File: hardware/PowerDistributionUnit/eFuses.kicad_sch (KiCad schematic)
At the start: 13 parts, among them U3 TCA9544A, U36 MCP23S17-E/SS

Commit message: schematic updated
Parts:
- removed C166: 0.1u, symbol Device:C_Small
- removed R134: R_Small, symbol Device:R_Small
- removed U36: MCP23S17-E/SS, Package_SO:SSOP-28_5.3x10.2mm_P0.65mm, symbol PowerDistributionUnitLib:MCP23S17-E/SS
- added J11, J12, J13, J18: Conn_01x02, Connector_PinHeader_2.54mm:PinHeader_1x02_P2.54mm_Vertical, symbol Connector_Generic:Conn_01x02
- C167: footprint (none) -> Capacitor_SMD:C_0603_1608Metric
- R121, R122, R123, R124, R125, R126, R127, R128: footprint (none) -> Resistor_SMD:R_0603_1608Metric
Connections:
- net SC0: now also J11.1 (Pin_1)
- net SC1: now also J12.1 (Pin_1)
- net SC2: now also J13.1 (Pin_1)
- net SC3: now also J18.1 (Pin_1)
- net SD0: now also J11.2 (Pin_2)
- net SD1: now also J12.2 (Pin_2)
- net SD2: now also J13.2 (Pin_2)
- net SD3: now also J18.2 (Pin_2)
- net R_{ILIM}_SCL renamed SDA
- net R_{ILIM}_SDA renamed SCL
- no-connect marks 9 -> 17
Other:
- removed sheet eFuseCAN
- added sheet eFuse Monitoring and Control (eFuse Monitoring and Control.kicad_sch)
- added sheet eFuse14 (eFuse.kicad_sch)
- added sheet eFuse15 (eFuse.kicad_sch)
- sheet eFuse0 ports: added IMON-; removed none
- sheet eFuse1 ports: added IMON-; removed none
- sheet eFuse10 ports: added IMON-; removed none
- sheet eFuse11 ports: added IMON-; removed none
- sheet eFuse12 ports: added IMON-; removed none
- sheet eFuse13 ports: added IMON-; removed none
- sheet eFuse2 ports: added IMON-; removed none
- sheet eFuse3 ports: added IMON-; removed none
- sheet eFuse4 ports: added IMON-; removed none
- sheet eFuse5 ports: added IMON-; removed none
- sheet eFuse6 ports: added IMON-; removed none
- sheet eFuse7 ports: added IMON-; removed none
- sheet eFuse8 ports: added IMON-; removed none
- sheet eFuse9 ports: added IMON-; removed none
- note added: "Control and Monitoring"
- note added: "Test Points"
- note removed: "0"
- note removed: "0011000"
- note removed: "0011010"
- note removed: "1"
- note removed: "1001100"
- note removed: "1001110"
- note removed: "AD0"
- note removed: "AD1"
- note removed: "ADDRESS"
- note removed: "Digital Pot not used in CAN output to maintain iso"
- note removed: "External Connections"
- note removed: "Output Enable"
- note removed: "R_{ILIM} I^{2}C Addresses"
- note removed: "to Connectors..."
- note removed: "to Control..."
- note removed: "to Monitoring..."
- company: (none) -> Longhorn Racing
- title: (none) -> eFuses
- moved on the sheet: R121, R122, R123, R124, R125, R126, R127, R128

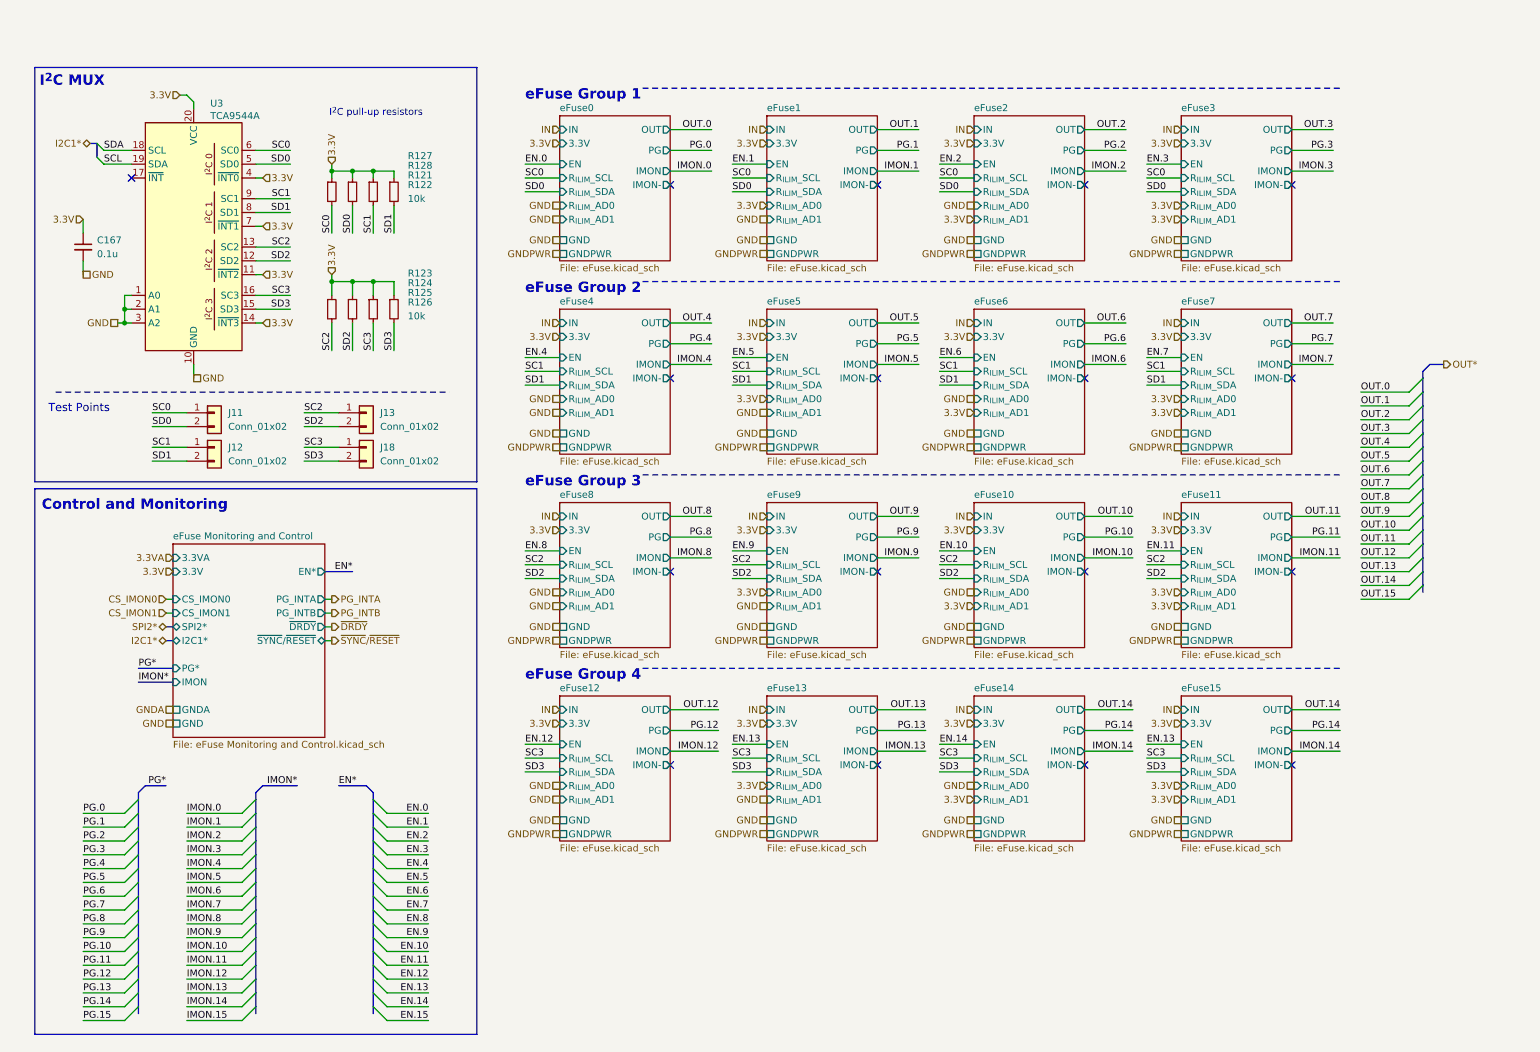
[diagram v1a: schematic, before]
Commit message: started layout for general and eFuses, corrected schematic (test point footprints, bus label names, connection points, etc.), corrected footprint courtyard (eFuse, diode)
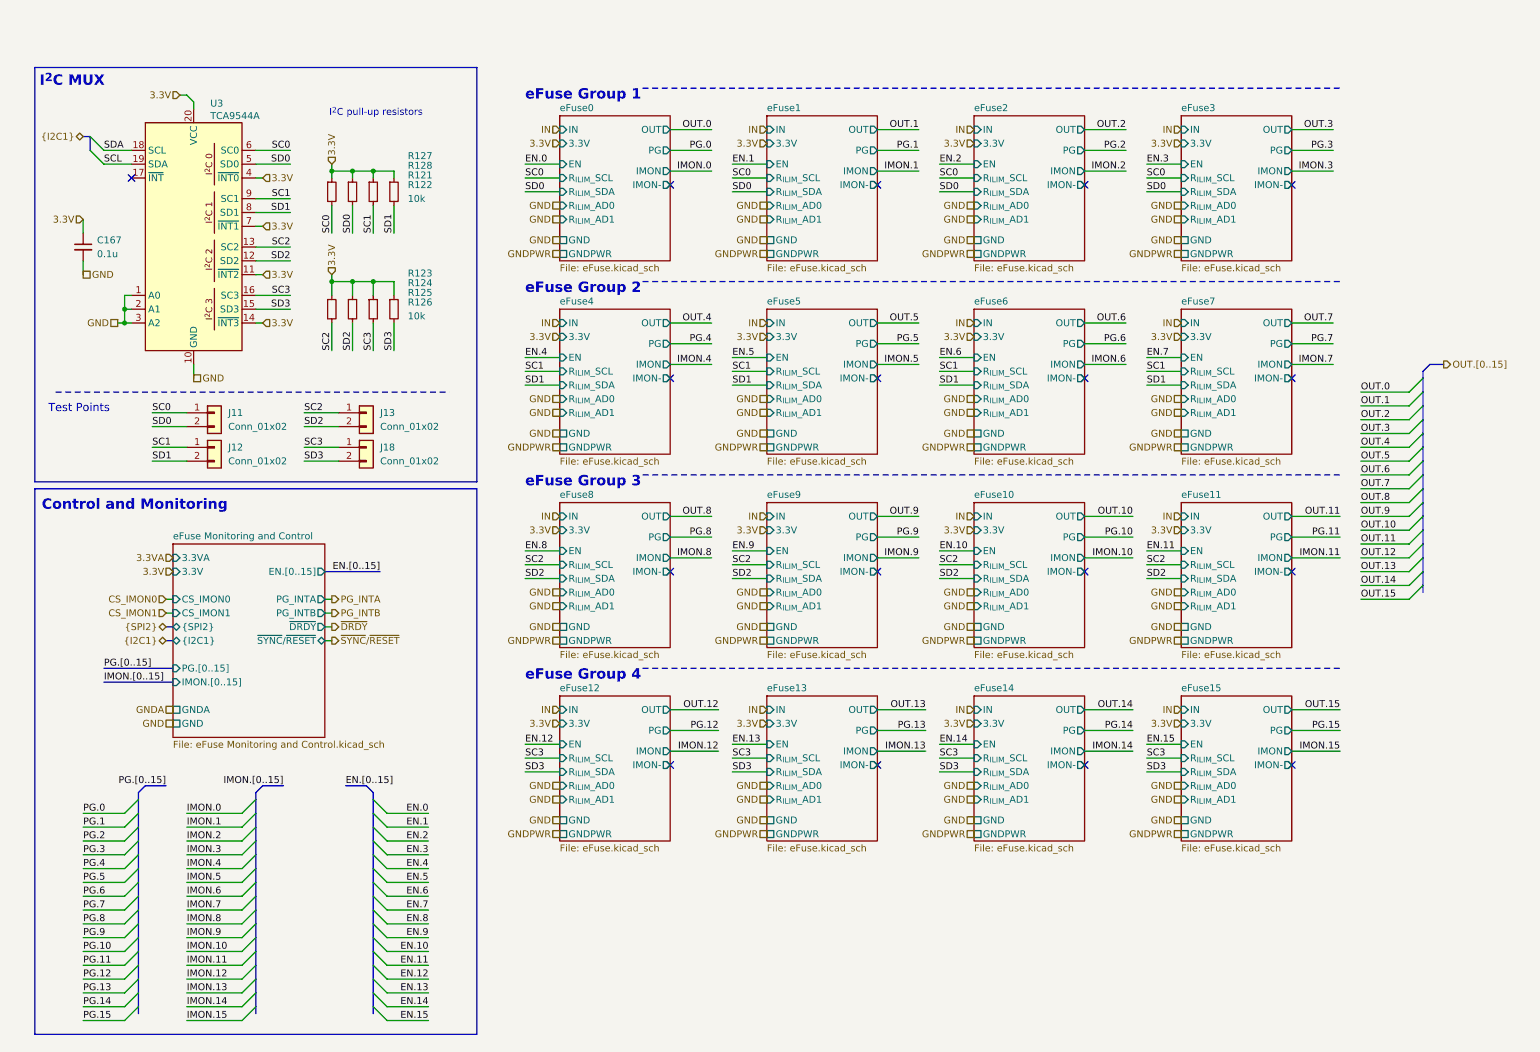
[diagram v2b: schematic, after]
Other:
- sheet eFuse Monitoring and Control ports: added EN.[0..15], IMON.[0..15], PG.[0..15], {I2C1}, {SPI2}; removed EN*, I2C1*, IMON, PG*, SPI2*

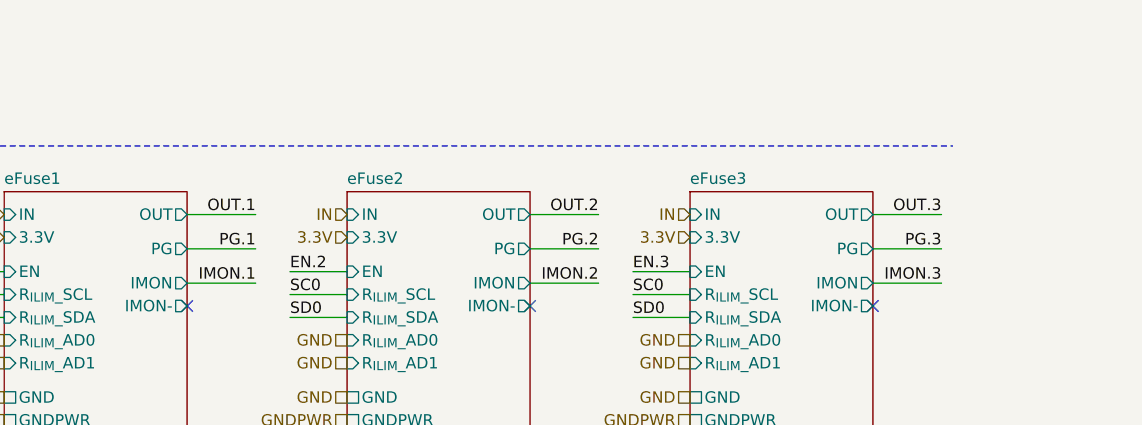
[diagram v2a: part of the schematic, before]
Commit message: Updated GND and 3.3V to GNDA and 3.3VA. Made progress on layout for current monitoring components
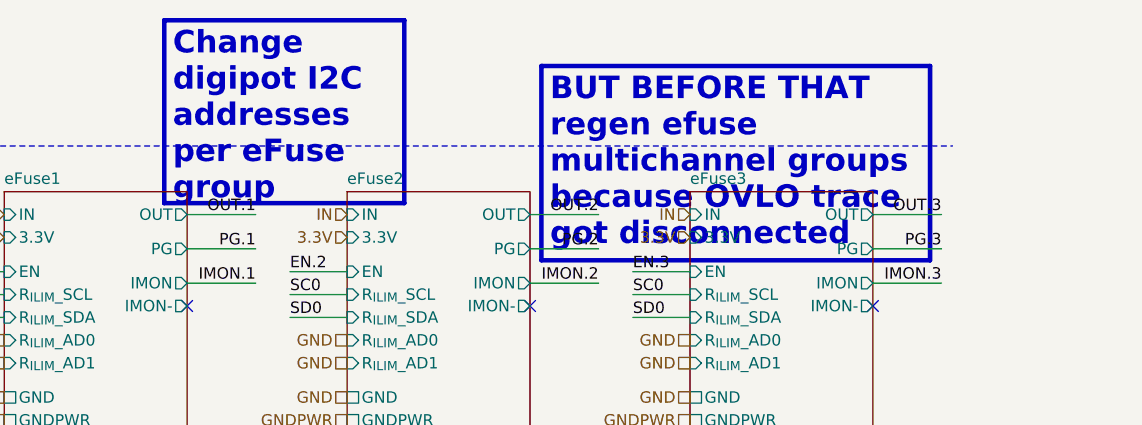
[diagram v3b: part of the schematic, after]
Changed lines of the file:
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@@
+		)
+	)
+	(text_box "Change digipot I2C addresses per eFuse group"
+		(exclude_from_sim no)
+		(at 168.91 5.08 0)
+		(size 26.67 20.32)
+		(margins 0.9525 0.9525 0.9525 0.9525)
+		(stroke
+			(width 0.5)
+			(type solid)
+			(color 255 0 0 1)
+		)
+		(fill
+			(type none)
+		)
+		(effects
+			(font
+				(size 2.5 2.5)
+				(thickness 0.254)
+				(bold yes)
+				(color 255 0 0 1)
+			)
+			(justify left top)
+		)
+	)
+	(text_box "BUT BEFORE THAT\nregen efuse multichannel groups because OVLO trace got disconnected"
+		(exclude_from_sim no)
+		(at 210.82 10.16 0)
+		(size 43.18 21.59)
+		(margins 0.9525 0.9525 0.9525 0.9525)
+		(stroke
+			(width 0.5)
+			(type solid)
+			(color 255 0 0 1)
+		)
+		(fill
+			(type none)
+		)
+		(effects
+			(font
+				(size 2.5 2.5)
+				(thickness 0.254)
+				(bold yes)
+				(color 255 0 0 1)
+			)
+			(justify left top)
 		)
 	)

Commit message: redid multichannel
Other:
- sheet eFuse0 ports: added none; removed R_{ILIM}_AD0, R_{ILIM}_AD1
- sheet eFuse1 ports: added none; removed R_{ILIM}_AD0, R_{ILIM}_AD1
- sheet eFuse10 ports: added none; removed R_{ILIM}_AD0, R_{ILIM}_AD1
- sheet eFuse11 ports: added none; removed R_{ILIM}_AD0, R_{ILIM}_AD1
- sheet eFuse12 ports: added none; removed R_{ILIM}_AD0, R_{ILIM}_AD1
- sheet eFuse13 ports: added none; removed R_{ILIM}_AD0, R_{ILIM}_AD1
- sheet eFuse14 ports: added none; removed R_{ILIM}_AD0, R_{ILIM}_AD1
- sheet eFuse15 ports: added none; removed R_{ILIM}_AD0, R_{ILIM}_AD1
- sheet eFuse2 ports: added none; removed R_{ILIM}_AD0, R_{ILIM}_AD1
- sheet eFuse3 ports: added none; removed R_{ILIM}_AD0, R_{ILIM}_AD1
- sheet eFuse4 ports: added none; removed R_{ILIM}_AD0, R_{ILIM}_AD1
- sheet eFuse5 ports: added none; removed R_{ILIM}_AD0, R_{ILIM}_AD1
- sheet eFuse6 ports: added none; removed R_{ILIM}_AD0, R_{ILIM}_AD1
- sheet eFuse7 ports: added none; removed R_{ILIM}_AD0, R_{ILIM}_AD1
- sheet eFuse8 ports: added none; removed R_{ILIM}_AD0, R_{ILIM}_AD1
- sheet eFuse9 ports: added none; removed R_{ILIM}_AD0, R_{ILIM}_AD1

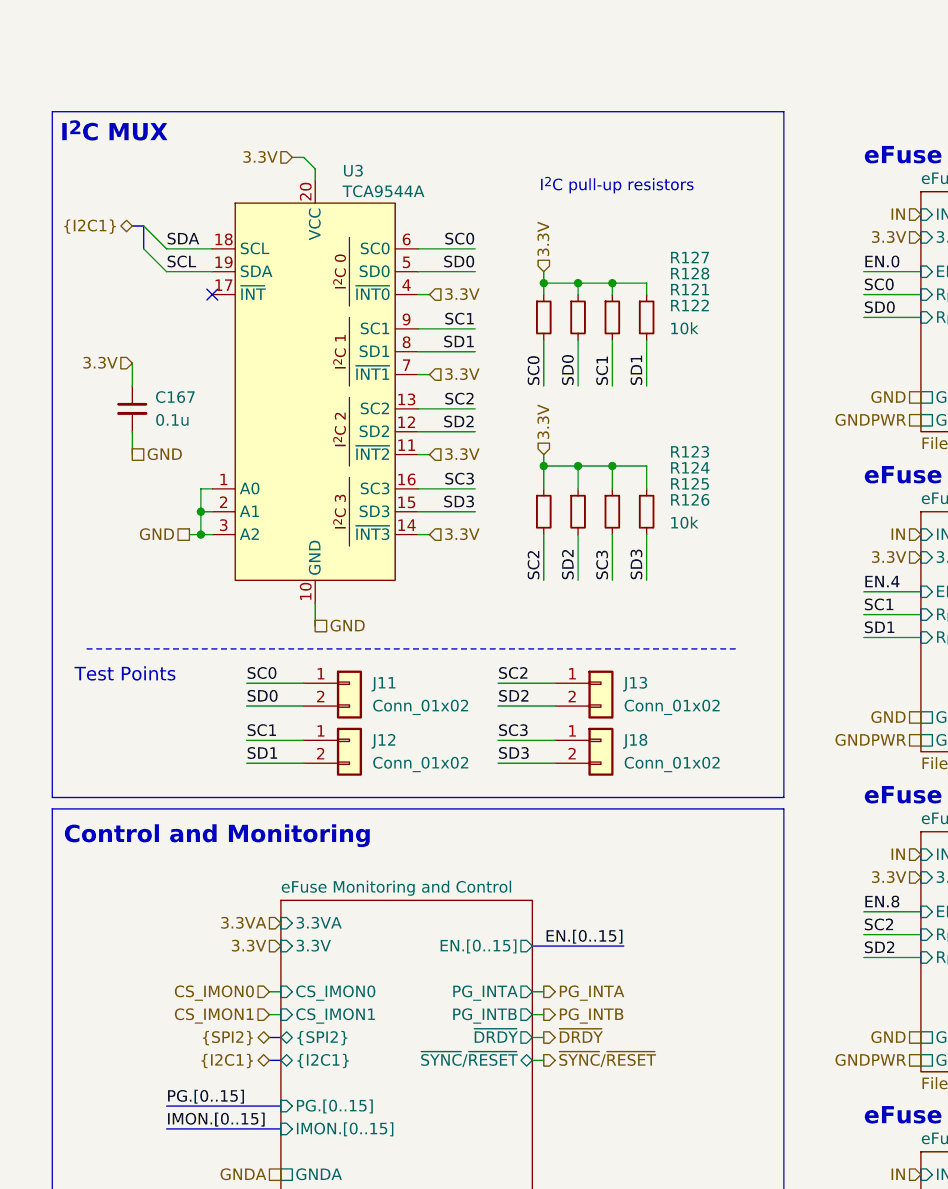
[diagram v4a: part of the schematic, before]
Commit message: test points, gnd net ties (added extra one), fixed drdy/sync mixup
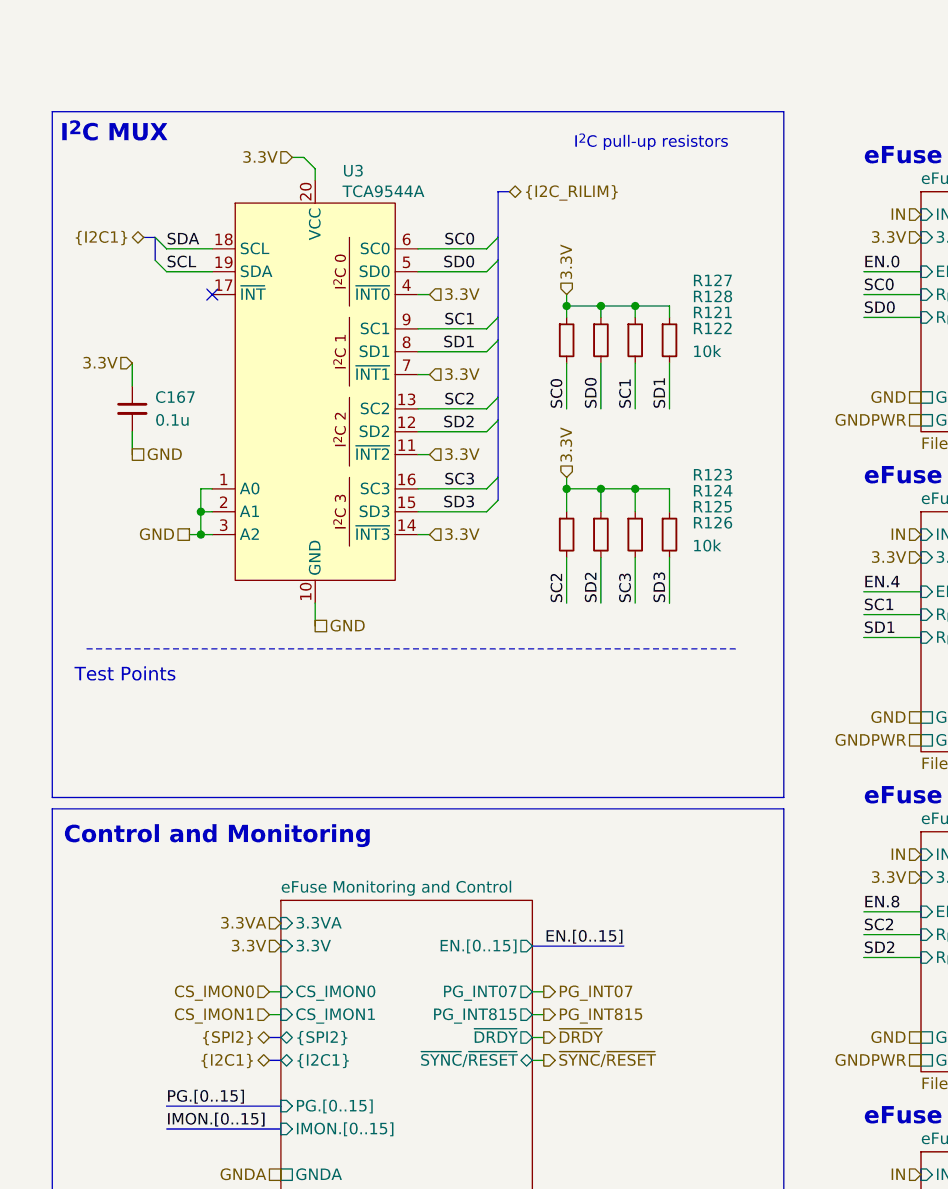
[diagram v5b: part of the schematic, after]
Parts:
- removed J11, J12, J13, J18: Conn_01x02, Connector_PinHeader_2.54mm:PinHeader_1x02_P2.54mm_Vertical, symbol Connector_Generic:Conn_01x02
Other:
- sheet eFuse Monitoring and Control ports: added PG_INT07, PG_INT815; removed PG_INTA, PG_INTB
- moved on the sheet: R121, R122, R123, R124, R125, R126, R127, R128
